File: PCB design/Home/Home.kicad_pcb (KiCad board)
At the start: 2 copper layers, 119.4 x 127 mm, 17 parts, among them J1 Fan, J2 LCD, J3 EM LOCK, J4 ACS712 Signal, J5 Power In, J7 RFID, J8 RFID, J9 LCD, U1 ACS712, U3 DHT11, U5 PIR, U6 MQ2

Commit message: PCB routed
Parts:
- moved J3 183.1 mm to (111.9, 40.6), turned to 0 degrees
- moved LM2596_buck_converter2 163.1 mm to (92.5, 39.6)
- moved BZ1 160.2 mm to (76.2, 132.2), turned to -90 degrees
- moved D1 155.5 mm to (91.4, 125.7)
- moved ESP32_DEVKIT_V1 110.0 mm to (116.8, 106.7), turned to 0 degrees
- moved LM2596_buck_converter1 109.0 mm to (106.4, 52.3), turned to 0 degrees
- moved J1 108.6 mm to (162.6, 45.7), turned to -90 degrees
- moved J7 107.8 mm to (162.6, 83.9)
- moved J8 107.8 mm to (162.6, 101.6)
- moved J2 107.8 mm to (162.6, 58.5)
- moved J9 107.7 mm to (162.6, 71.2)
- moved U3 103.6 mm to (63.5, 121.9)
- moved U5 88.5 mm to (89.4, 106.4), turned to -90 degrees
- moved U1 82.8 mm to (149.6, 81.5)
- moved J5 81.5 mm to (129.5, 40.6)
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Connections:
- ESP32_DEVKIT_V1 pad 10: unconnected-(ESP32_DEVKIT_V1-GPIO27-Pad10) -> BUZZ
- ESP32_DEVKIT_V1 pad 11: BLUE -> RED
- ESP32_DEVKIT_V1 pad 12: GREEN -> BLUE
- ESP32_DEVKIT_V1 pad 13: RED -> GREEN
- ESP32_DEVKIT_V1 pad 21: DHT -> unconnected-(ESP32_DEVKIT_V1-GPIO16/RXD_2-Pad21)
- ESP32_DEVKIT_V1 pad 24: RELAY -> ACS
- ESP32_DEVKIT_V1 pad 26: unconnected-(ESP32_DEVKIT_V1-GPIO21/SDA-Pad26) -> SDA
- ESP32_DEVKIT_V1 pad 4: ACS -> unconnected-(ESP32_DEVKIT_V1-GPIO34-Pad4)
- ESP32_DEVKIT_V1 pad 7: SDA -> RELAY
- ESP32_DEVKIT_V1 pad 8: BUZZ -> unconnected-(ESP32_DEVKIT_V1-GPIO25-Pad8)
- ESP32_DEVKIT_V1 pad 9: unconnected-(ESP32_DEVKIT_V1-GPIO26-Pad9) -> DHT
- J1 pad 1: 5V -> GND
- J1 pad 2: -5V -> +5V
- J2 pad 1: 5V -> GND
- J2 pad 2: -5V -> +5V
- J3 pad 1: 12V -> RELAY
- J3 pad 2: GND -> -12V
- J3 pad 3: RELAY -> +12V
- J4 pad 1: IP+ -> -12V
- J4 pad 2: -12V -> unconnected-(J4-Pin_2-Pad2)
- J5 pad 1: +12V -> -12V
- J5 pad 2: -12V -> +12V
- J7 pad 1: MISO -> SCK
- J7 pad 2: MOSI -> SDA
- J7 pad 3: SCK -> MISO
- J8 pad 1: SDA -> GND
- J8 pad 2: 3.3V -> +3.3V
- J8 pad 3: GND -> MOSI
- U3 pad 1: 3V3 -> +3.3V
- U5 pad 3: 3V3 -> +3.3V
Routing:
- net GND: track 0.00 -> 425.1 mm
- net +3.3V: track 0.00 -> 270.6 mm
- net -12V: track 0.00 -> 129.3 mm
- net +5V: track 0.00 -> 125.0 mm
- net MOSI: track 0.00 -> 121.9 mm
- net PIR: track 0.00 -> 88.6 mm
- net +12V: track 0.00 -> 82.9 mm
- net RELAY: track 0.00 -> 69.0 mm
- net SDA: track 0.00 -> 57.8 mm
- net SCK: track 0.00 -> 51.3 mm
- net DHT: track 0.00 -> 48.1 mm
- net BUZZ: track 0.00 -> 38.5 mm
- net MISO: track 0.00 -> 37.1 mm
- net RED: track 0.00 -> 18.6 mm
- net BLUE: track 0.00 -> 17.9 mm
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- added copper zone on B.Cu, net GND
- added copper zone on F.Cu, net GND
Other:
- board size 119.4 x 127 mm -> 119.4 x 121.9 mm

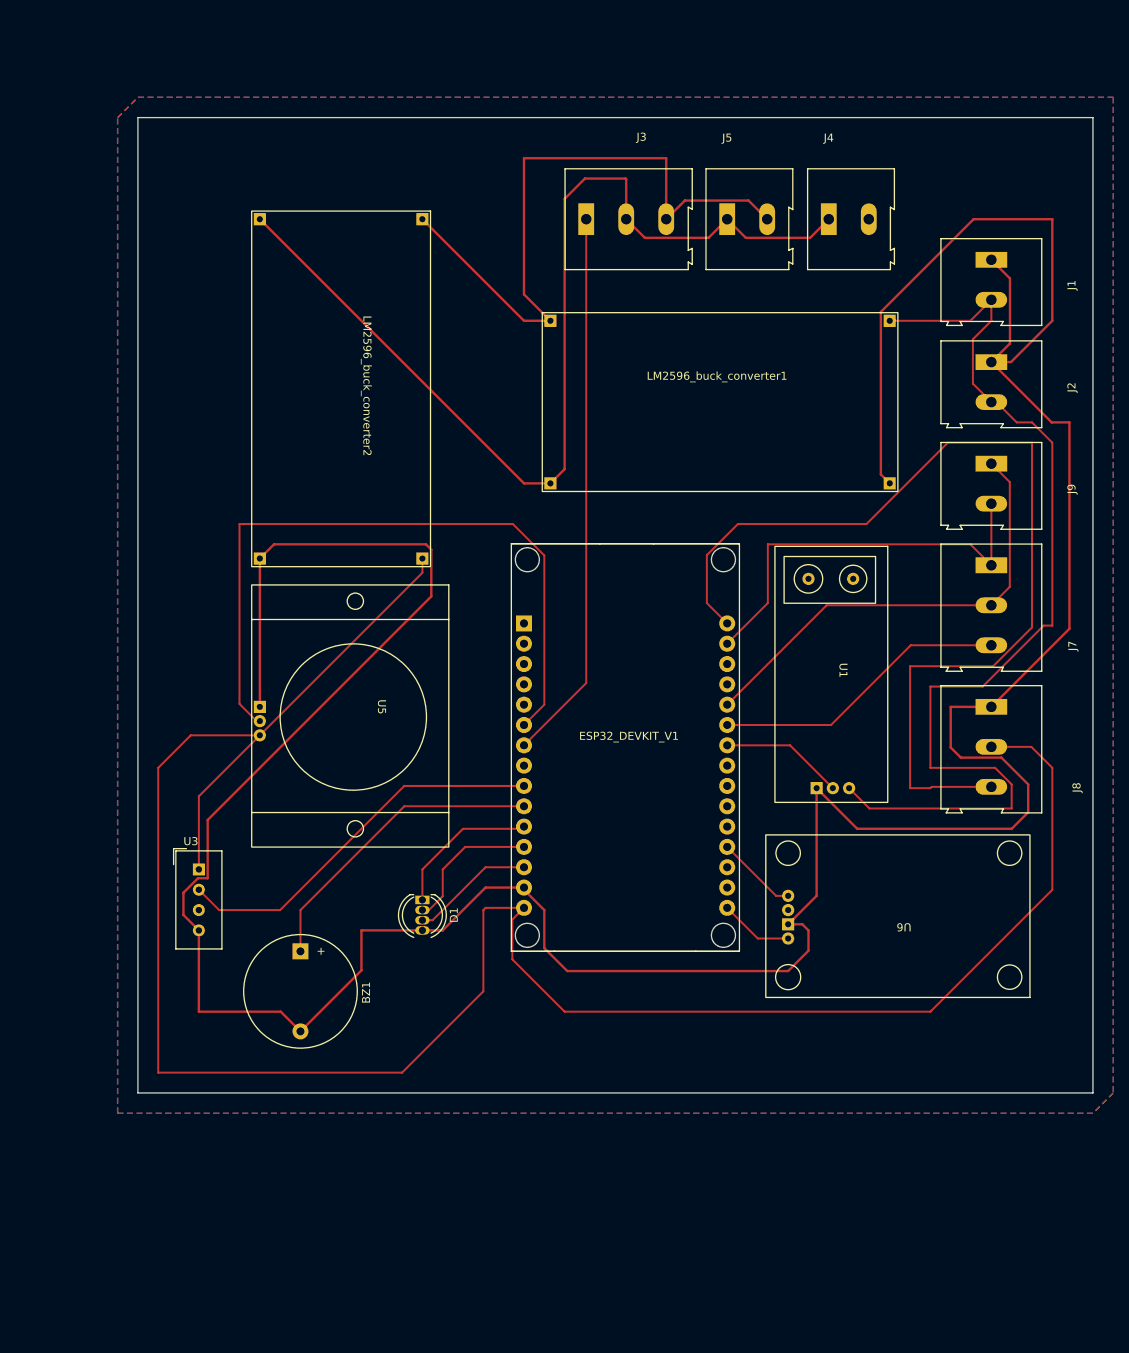
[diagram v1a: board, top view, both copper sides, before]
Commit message: PCB rerouting, with warnings
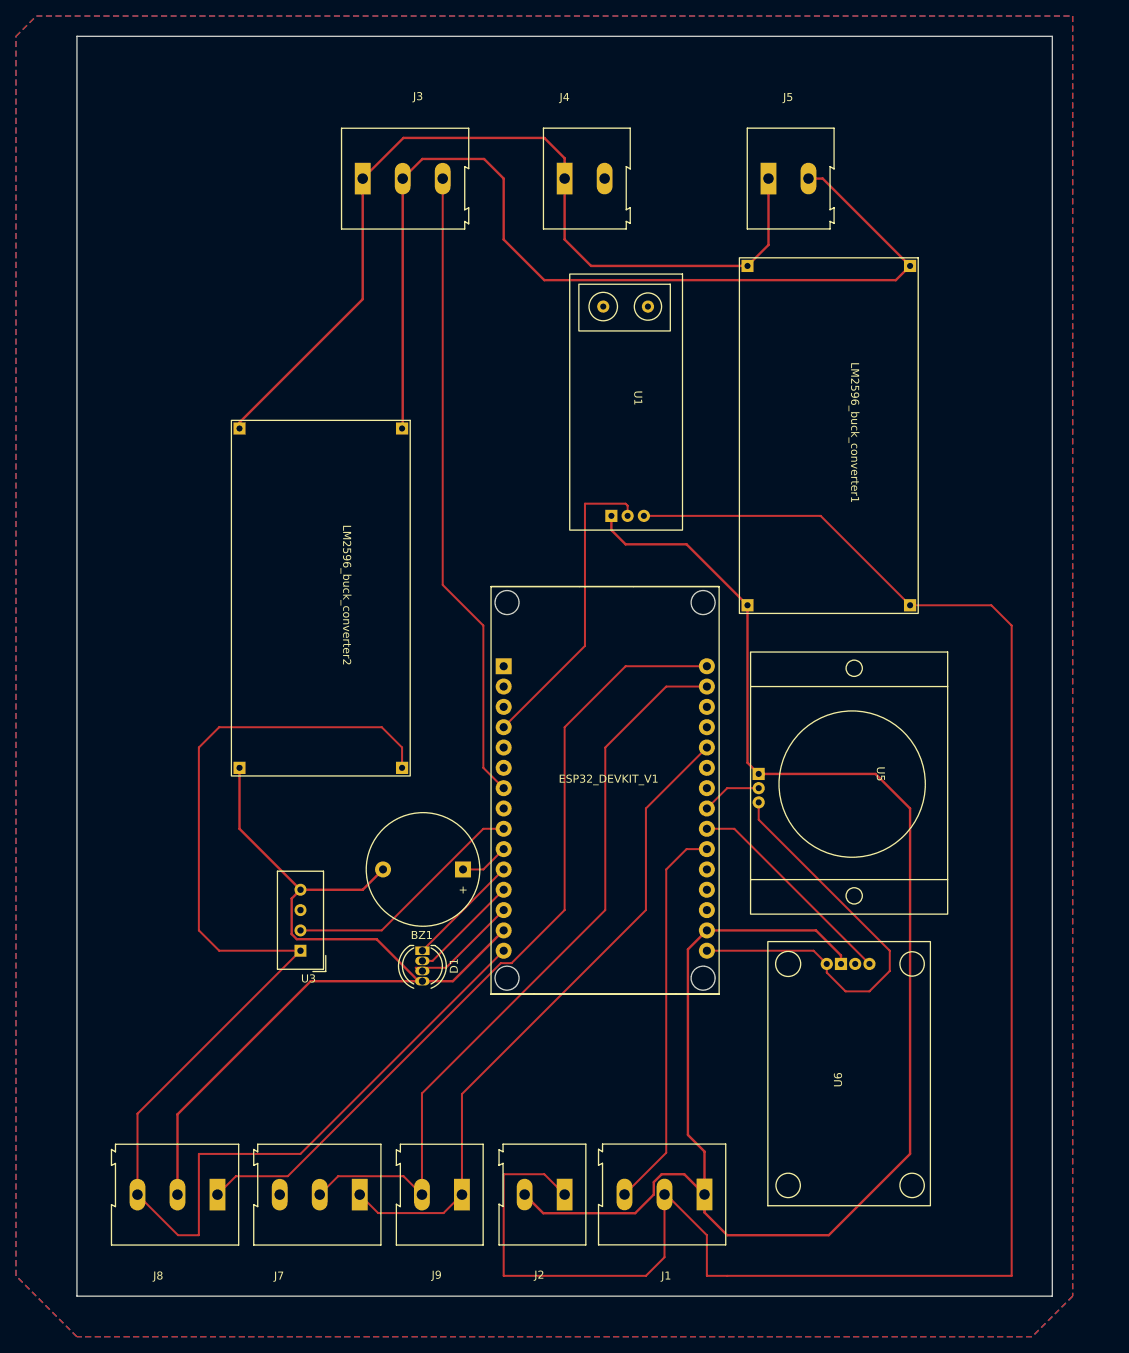
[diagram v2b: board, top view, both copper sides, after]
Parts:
- J1: footprint TerminalBlock:TerminalBlock_Altech_AK300-2_P5.00mm -> TerminalBlock:TerminalBlock_Altech_AK300-3_P5.00mm
- LM2596_buck_converter1: value ~ -> 5V
- LM2596_buck_converter2: value ~ -> 3.3V
- moved J1 122.2 mm to (126.7, 162.6), turned to 180 degrees
- moved J2 116.9 mm to (109.2, 162.6), turned to 180 degrees
- moved J8 114.3 mm to (65.8, 162.6), turned to 180 degrees
- moved J9 112.8 mm to (96.4, 162.6), turned to 180 degrees
- moved J7 111.5 mm to (83.6, 162.6), turned to 180 degrees
- moved U5 62.9 mm to (151.8, 114.8)
- moved LM2596_buck_converter1 47.5 mm to (153.4, 45.5), turned to -90 degrees
- moved U1 42.6 mm to (124.0, 47.5)
- moved U6 41.9 mm to (134.6, 164.0), turned to 90 degrees
- moved J4 33.4 mm to (109.2, 35.6)
- moved J3 28.4 mm to (84.0, 35.6)
- moved LM2596_buck_converter2 26.3 mm to (89.9, 65.8)
- moved BZ1 22.8 mm to (96.5, 121.9), turned to 180 degrees
- moved U3 16.3 mm to (76.2, 132.1), turned to 180 degrees
- moved J5 7.24 mm to (134.7, 35.6)
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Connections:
- ESP32_DEVKIT_V1 pad 17: unconnected-(ESP32_DEVKIT_V1-GND-Pad17) -> GND
- ESP32_DEVKIT_V1 pad 19: MQ2 -> unconnected-(ESP32_DEVKIT_V1-GPIO2-Pad19)
- ESP32_DEVKIT_V1 pad 21: unconnected-(ESP32_DEVKIT_V1-GPIO16/RXD_2-Pad21) -> Fan
- ESP32_DEVKIT_V1 pad 22: unconnected-(ESP32_DEVKIT_V1-GPIO17/TXD_2-Pad22) -> MQ2
- ESP32_DEVKIT_V1 pad 23: unconnected-(ESP32_DEVKIT_V1-GPIO5/SS-Pad23) -> PIR
- ESP32_DEVKIT_V1 pad 24: ACS -> unconnected-(ESP32_DEVKIT_V1-GPIO18/SCK-Pad24)
- ESP32_DEVKIT_V1 pad 4: unconnected-(ESP32_DEVKIT_V1-GPIO34-Pad4) -> ACS
- ESP32_DEVKIT_V1 pad 6: PIR -> unconnected-(ESP32_DEVKIT_V1-GPIO32-Pad6)
- J2 pad 1: GND -> +5V
- J2 pad 2: +5V -> GND
- J3 pad 1: RELAY -> -12V
- J3 pad 2: -12V -> +12V
- J3 pad 3: +12V -> RELAY
- J7 pad 1: SCK -> SDA
- J7 pad 2: SDA -> SCK
- J7 pad 3: MISO -> unconnected-(J7-Pin_3-Pad3)
- J8 pad 1: GND -> MOSI
- J8 pad 2: +3.3V -> GND
- J8 pad 3: MOSI -> +3.3V
- U5 pad 3: +3.3V -> 3V3
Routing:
- net +5V: track 125.0 -> 233.8 mm
- net +3.3V: track 270.6 -> 174.1 mm
- net GND: track 425.1 -> 337.9 mm
- net PIR: track 88.6 -> 7.53 mm
- net Fan: track 0.00 -> 48.9 mm
- net 3V3: track 9.21 -> 54.5 mm
- net SCK: track 51.3 -> 95.9 mm
- net +12V: track 82.9 -> 124.4 mm
- net MISO: track 37.1 -> 0.00 mm
- net BUZZ: track 38.5 -> 6.13 mm
- net SDA: track 57.8 -> 83.3 mm
- net ACS: track 15.4 -> 38.9 mm
- net MOSI: track 121.9 -> 101.9 mm
- net DHT: track 48.1 -> 30.7 mm
- net MQ2: track 10.2 -> 27.3 mm
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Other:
- board size 119.4 x 121.9 mm -> 121.9 x 157.5 mm
